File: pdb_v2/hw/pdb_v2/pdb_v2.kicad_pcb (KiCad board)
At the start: 4 copper layers, 92.7 x 64.9 mm, 70 parts, among them J1 XT30-M_Ver, J2 JST-PH_01x02, J3 Conn_01x06_Pin, J5 JST-PH_01x02, J6 Conn_01x03, J7 Conn_01x03, J8 Conn_01x04, Q1 60Vds, SW1 SW_Push, SW2 SW_Push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

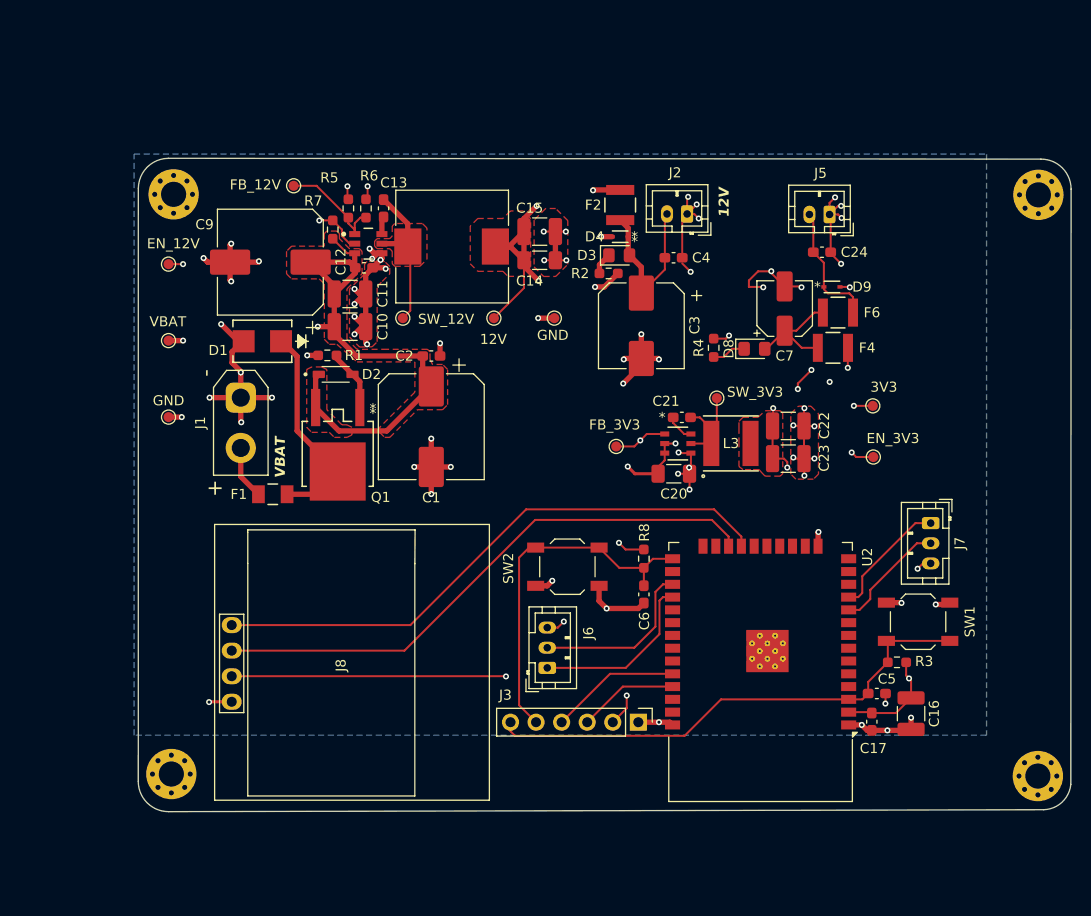
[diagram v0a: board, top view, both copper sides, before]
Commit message: added 2 leds on esp32, moved components
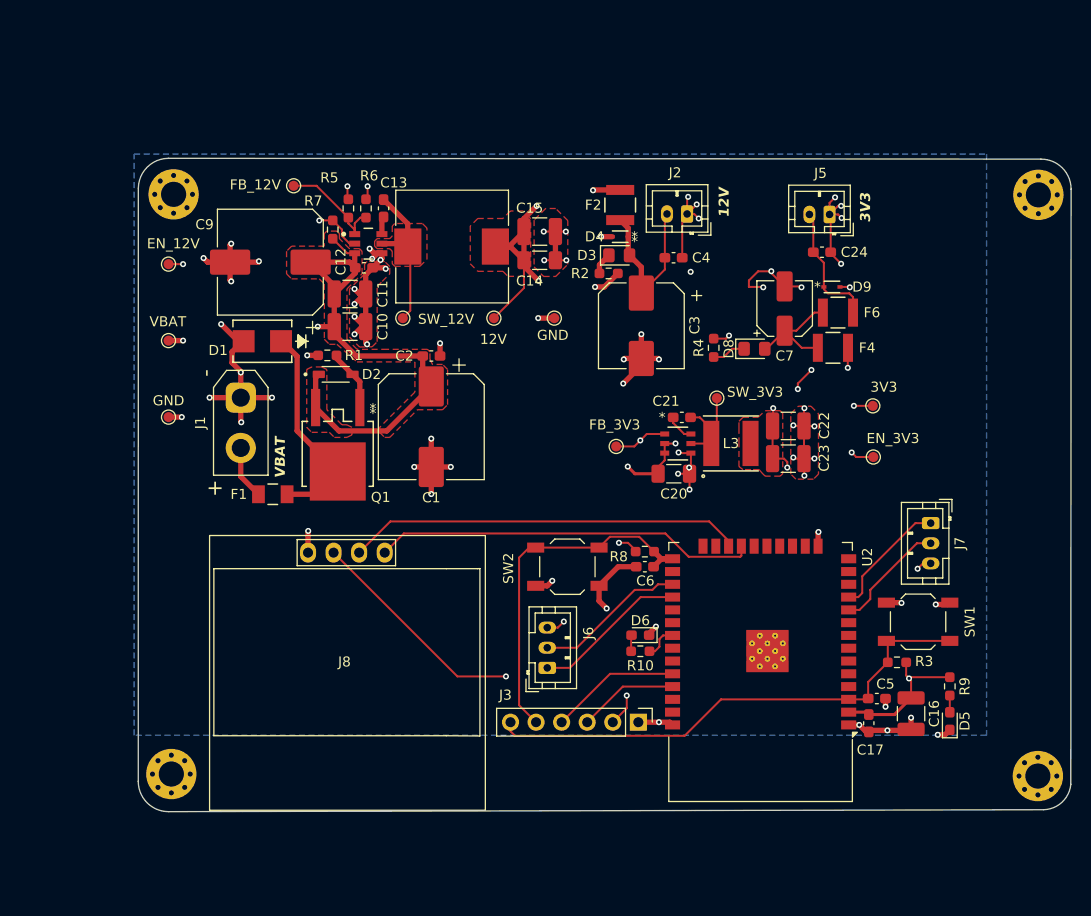
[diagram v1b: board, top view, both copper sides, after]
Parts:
- added D5: LED, LED_SMD:LED_0603_1608Metric_Pad1.05x0.95mm_HandSolder, F.Cu at (92.7, 67.9)
- added D6: LED, LED_SMD:LED_0603_1608Metric_Pad1.05x0.95mm_HandSolder, F.Cu at (61.9, 59.4)
- added R10: 1k, Resistor_SMD:R_0603_1608Metric_Pad0.98x0.95mm_HandSolder, F.Cu at (61.9, 61.0)
- added R9: 1k, Resistor_SMD:R_0603_1608Metric_Pad0.98x0.95mm_HandSolder, F.Cu at (92.7, 64.5)
- moved C6 2.75 mm to (62.4, 52.6), turned to 180 degrees
- moved J8 0.85 mm to (32.5, 61.8), turned to 0 degrees
- moved R8 0.71 mm to (62.4, 51.1), turned to 0 degrees
- moved C5 0.50 mm to (85.4, 65.7)
- moved C17 0.34 mm to (84.6, 68.2)
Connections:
- U2 pad 31: unconnected-(U2-IO19-Pad31) -> Net-(U2-IO19)
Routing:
- net /OLED SDA: track 57.5 -> 38.2 mm
- net /OLED SCL: track 56.4 -> 39.3 mm
- net Net-(U2-IO19): track 0.00 -> 3.39 mm
- net /BMS RX: track 17.1 -> 15.1 mm
- net /BMS TX: track 17.3 -> 15.4 mm
- net GND: track 165.4 -> 167.2 mm, vias 73 -> 75
- net Net-(D5-A): track 0.00 -> 1.66 mm
- net Net-(D6-A): track 0.00 -> 1.62 mm
- net 3V3_BUS: track 158.2 -> 157.1 mm
- net /BOOT: track 35.7 -> 36.3 mm
- net 12V_BUS: track 120.3 -> 119.8 mm, vias 8 -> 7
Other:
- board text added: "3V3"

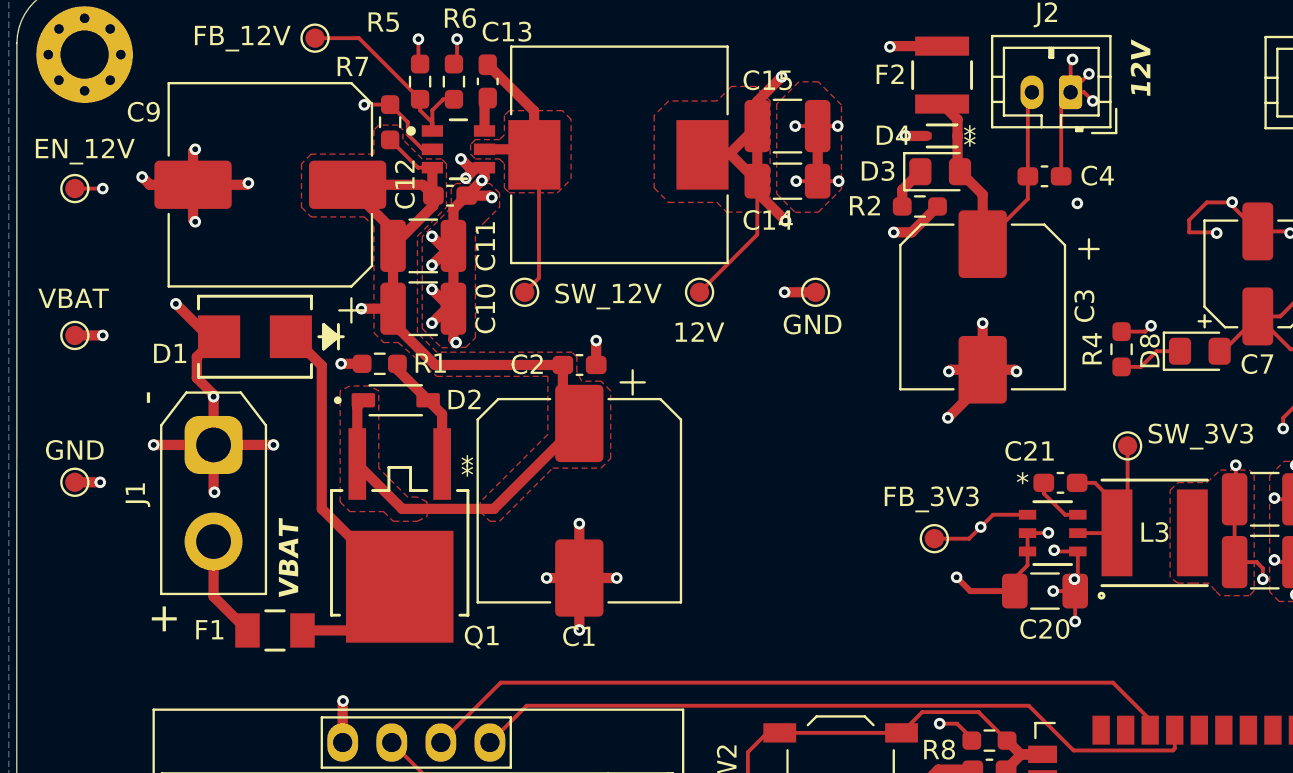
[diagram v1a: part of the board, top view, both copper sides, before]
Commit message: changed J1 footprint
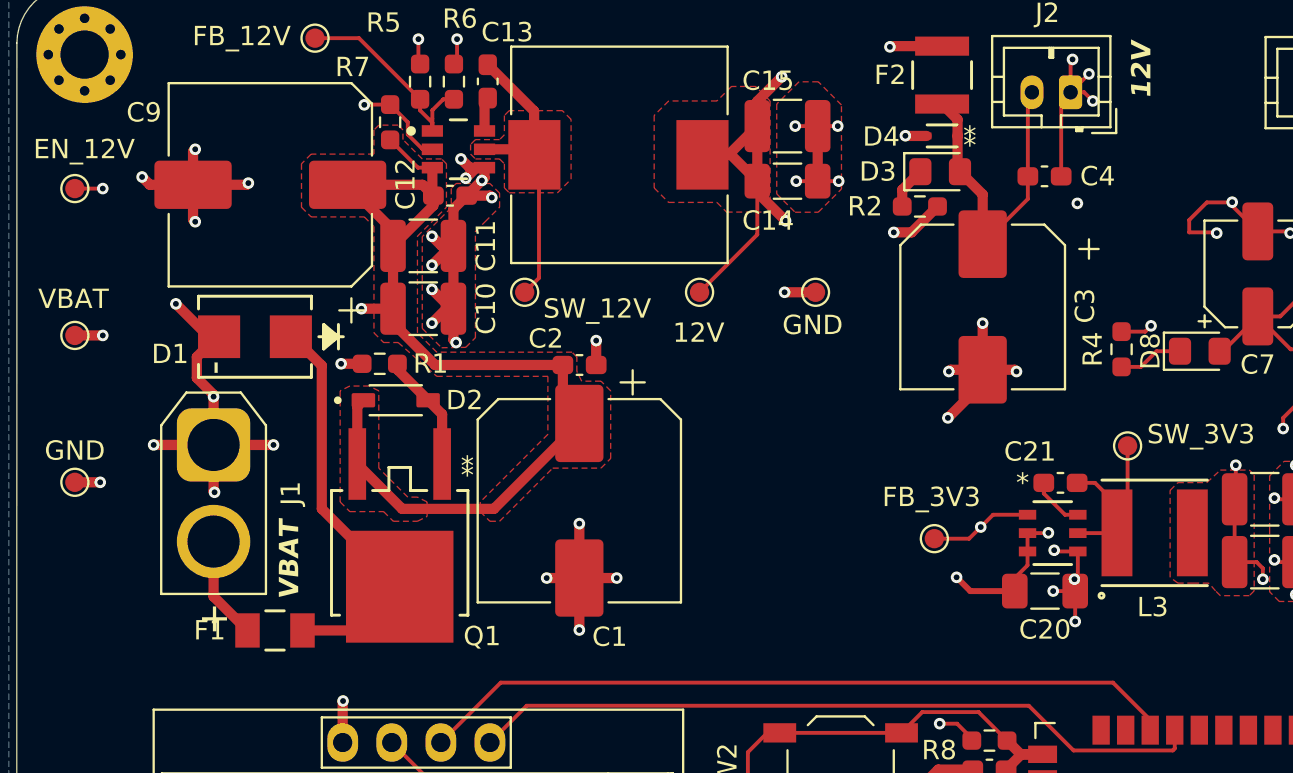
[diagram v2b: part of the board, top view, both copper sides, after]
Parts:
- J1: footprint Connector_AMASS:AMASS_XT30UPB-M_1x02_P5.0mm_Vertical -> Connector_AMASS:AMASS_XT30U-M_1x02_P5.0mm_Vertical
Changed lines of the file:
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@@
 		)
 	)
-	(footprint "Connector_AMASS:AMASS_XT30UPB-M_1x02_P5.0mm_Vertical"
+	(footprint "Connector_AMASS:AMASS_XT30U-M_1x02_P5.0mm_Vertical"
 		(layer "F.Cu")
 		(at 22.2 35.8 -90)
-		(descr "Connector XT30 Vertical PCB Male, https://www.tme.eu/Document/e5863b891432488e7531b3c4468225ac/XT30PB-M.pdf")
+		(descr "Connector XT30 Vertical Cable Male, https://www.tme.eu/Document/7d9d972ae3468777f69ec2ee99897652/XT30U-M.pdf")
 		(tags "RC Connector XT30")
 		(property "Reference" "J1"
-			(at 2.5 4.014998 90)
+			(at 2.5 -4 270)
 			(layer "F.SilkS")
 			(effects
@@
 		)
 		(property "Value" "XT30-M_Ver"
-			(at 2.5 4 90)
+			(at 2.5 4 270)
 			(layer "F.Fab")
 			(effects
@@
 		)
 		(fp_text user "+"
-			(at 9 2.6 90)
+			(at 9 0 270)
 			(layer "F.SilkS")
 			(effects
@@
 		)
 		(fp_text user "-"
-			(at -2.45 3.5 90)
+			(at -4 0 270)
 			(layer "F.SilkS")
 			(effects
@@
 		)
 		(fp_text user "${REFERENCE}"
-			(at 2.5 0 90)
+			(at 2.5 0 270)
 			(layer "F.Fab")
 			(effects
@@
 		(pad "1" thru_hole roundrect
 			(at 0 0 270)
-			(size 3 3)
-			(drill 1.8)
+			(size 3.8 3.8)
+			(drill 2.7)
 			(layers "*.Cu" "*.Mask")
 			(remove_unused_layers no)
-			(roundrect_rratio 0.25)
+			(roundrect_rratio 0.2)
 			(net 2 "GND")
 			(pinfunction "Pin_1")
@@
 		(pad "2" thru_hole circle
 			(at 5 0 270)
-			(size 3 3)
-			(drill 1.8)
+			(size 3.8 3.8)
+			(drill 2.7)
 			(layers "*.Cu" "*.Mask")
 			(remove_unused_layers no)
@@
 		)
 		(embedded_fonts no)
-		(model "C:/Users/Leo/Downloads/Amass_XT30UPB-M.step"
+		(model "${KICAD9_3DMODEL_DIR}/Connector_AMASS.3dshapes/AMASS_XT30U-M_1x02_P5.0mm_Vertical.step"
 			(offset
-				(xyz 2.5 0 0)
+				(xyz 0 0 0)
 			)
 			(scale
@@
 			)
 			(rotate
-				(xyz -0 -0 -0)
+				(xyz 0 0 0)
 			)
 		)
@@
 		(tags "capacitor electrolytic")
 		(property "Reference" "C1"
-			(at 7.05 0 180)
+			(at 7.05 -1.572502 180)
 			(layer "F.SilkS")
 			(effects
@@
 		(tags "capacitor handsolder")
 		(property "Reference" "C2"
-			(at -2.677498 0 0)
+			(at -1.7375 -1.3625 0)
 			(layer "F.SilkS")
 			(effects
@@
 		)
 		(property "Value" "SW_12V"
-			(at 4.3 0.1 0)
+			(at 3.75 0.85 0)
 			(layer "F.SilkS")
 			(effects
@@
 		(tags "ESD5Z12T1G ")
 		(property "Reference" "D4"
-			(at 2.5501 0 0)
+			(at 3.15 -0.0403 0)
 			(unlocked yes)
 			(layer "F.SilkS")
@@
 		(tags "74404052039 ")
 		(property "Reference" "L3"
-			(at 0 0 0)
+			(at -0.1 3.85 0)
 			(unlocked yes)
 			(layer "F.SilkS")

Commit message: final changes for pcb
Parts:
- H1, H2, H3, H4: footprint MountingHole:MountingHole_2.5mm_Pad_Via -> MountingHole:MountingHole_2.5mm_Pad
- moved H2 66.3 mm to (95.1, 81.6)
- moved H4 58.2 mm to (95.1, 15.5)
- moved G*** 16.2 mm to (55.0, 40.5)
- moved H3 8.50 mm to (15.5, 81.7)
- moved C5 6.37 mm to (79.3, 67.5)
- moved C6 6.37 mm to (56.2, 54.4)
- moved D5 6.37 mm to (86.5, 69.7)
- moved J3 6.37 mm to (55.6, 69.8)
- moved J7 6.37 mm to (84.6, 50.0)
- moved R3 6.37 mm to (81.3, 63.9)
- moved R8 6.37 mm to (56.2, 52.9)
- moved R9 6.37 mm to (86.5, 66.2)
- moved SW1 6.37 mm to (83.4, 59.8)
- moved J8 6.37 mm to (26.4, 63.5)
- moved D6 6.37 mm to (55.8, 61.1)
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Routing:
- net 12V_BUS: track 119.8 -> 131.2 mm
- net 3V3_BUS: track 157.1 -> 167.2 mm
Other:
- board size 92.7 x 64.9 mm -> 86.4 x 73.3 mm
- board text added: "Power Distribution Board V2 for F25 Skateboard by Leopoldo Mendoza, Mike Yao, Arnav Shah"
- board text removed: "Power Distribution Board v1 for F25 Skateboard by Leopoldo Mendoza"

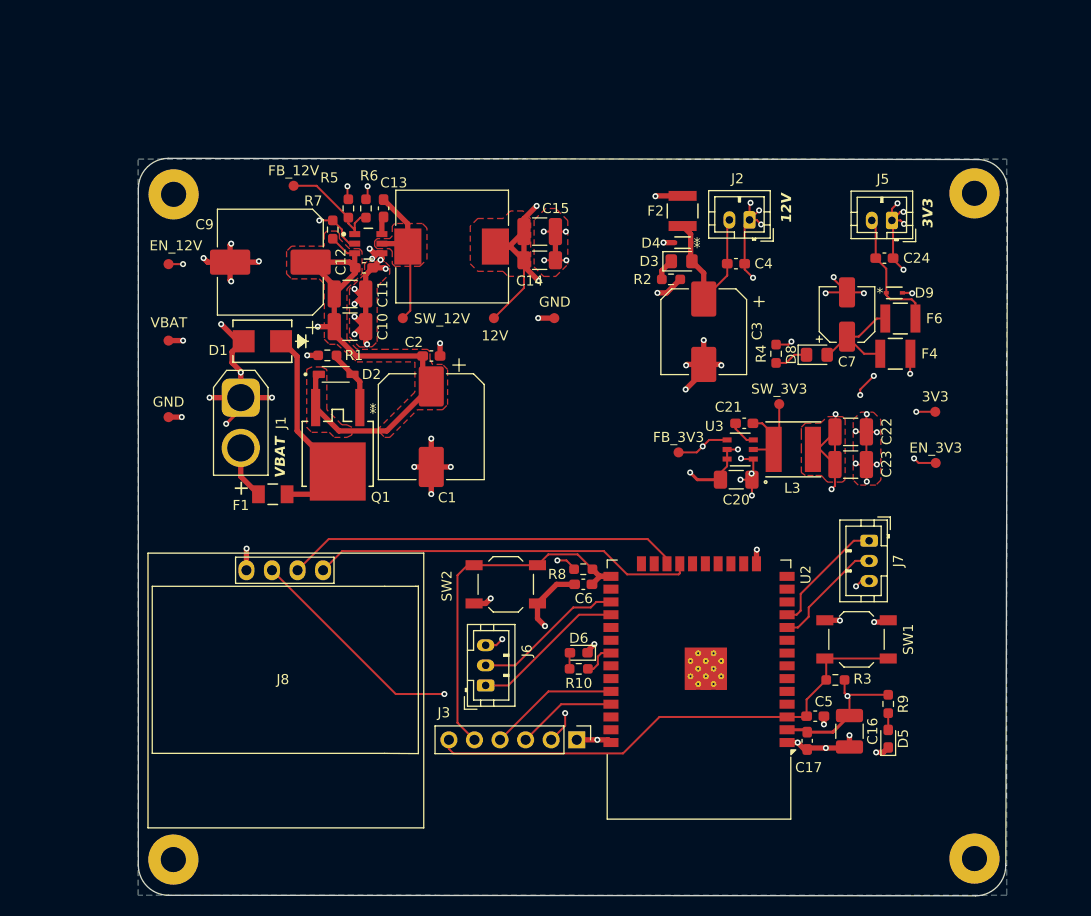
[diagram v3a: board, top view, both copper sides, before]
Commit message: added silkscreen
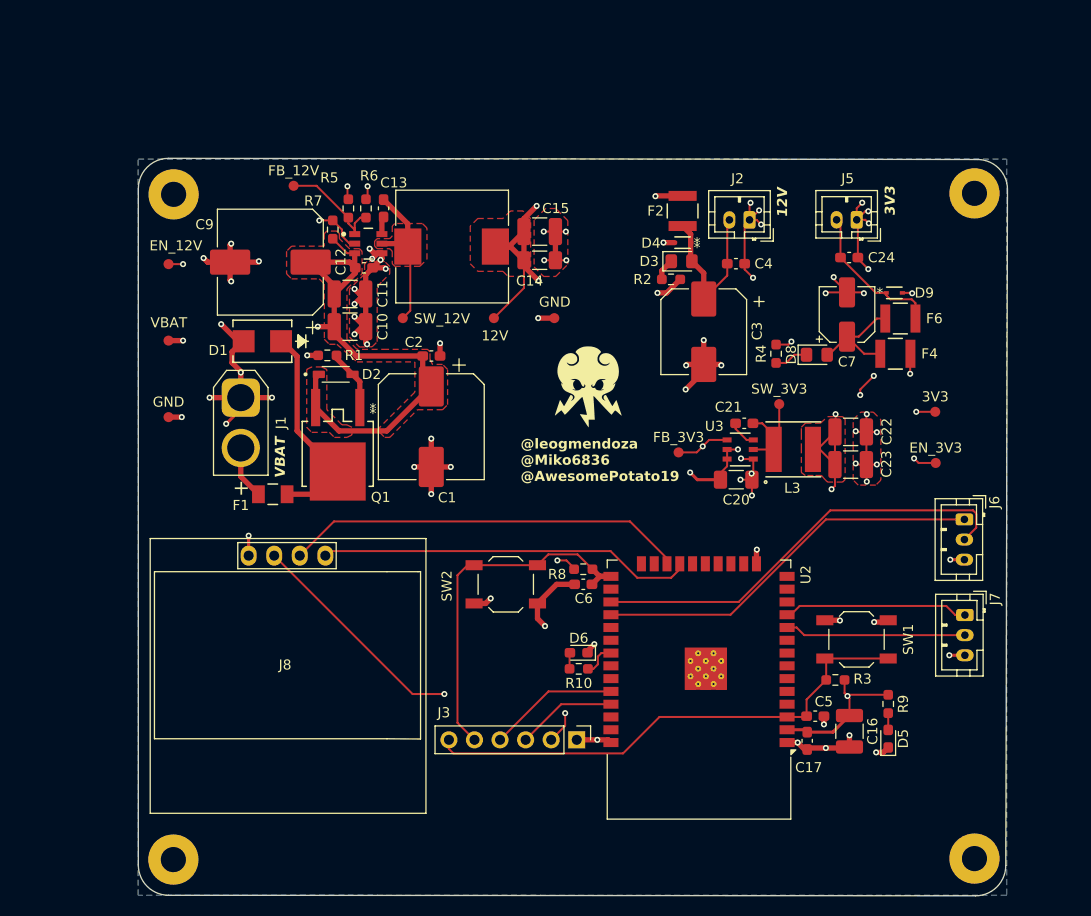
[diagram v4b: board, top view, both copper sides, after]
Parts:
- added G***: LOGO, LOGO, F.Cu at (56.7, 34.7)
- moved J6 50.4 mm to (94.1, 47.9), turned to -90 degrees
- moved J7 12.0 mm to (94.2, 57.4)
- moved C24 3.50 mm to (82.7, 21.9)
- moved J5 3.50 mm to (83.4, 18.1)
- moved G*** 2.00 mm to (55.0, 38.5)
- moved J8 1.47 mm to (26.6, 62.1)
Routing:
- net /BMS RX: track 15.1 -> 43.3 mm
- net /BMS TX: track 15.4 -> 39.0 mm
- net /VESC RX: track 11.4 -> 18.0 mm
- net /VESC TX: track 12.2 -> 18.4 mm
- net Net-(J5-Pin_2): track 12.8 -> 14.9 mm
- net /OLED SDA: track 38.2 -> 37.4 mm
- net GND: track 167.2 -> 166.6 mm
- net /OLED SCL: track 39.3 -> 40.0 mm
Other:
- board text added: "@leogmendoza @Miko6836 @AwesomePotato19"

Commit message: changed silkscreen on back of board
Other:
- board text added: "Power Distribution + Telemetry Board v2 for F25 Skateboard by Leopoldo Mendoza, Mike Yao, Arnav Shah"
- board text removed: "Power Distribution Board V2 for F25 Skateboard by Leopoldo Mendoza, Mike Yao, Arnav Shah"

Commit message: Layout Update
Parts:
- moved J3 38.6 mm to (19.0, 57.4), turned to 0 degrees
- moved C20 8.76 mm to (80.2, 43.8)
- moved C21 8.76 mm to (81.0, 38.2)
- moved C22 8.76 mm to (91.6, 39.1)
- moved C23 8.76 mm to (91.6, 42.3)
- moved C7 8.76 mm to (91.2, 27.4)
- moved D3 8.76 mm to (74.8, 22.1)
- moved D4 8.76 mm to (74.9, 20.2)
- moved D8 8.76 mm to (88.2, 31.4)
- moved EN_3V3 8.76 mm to (100.0, 42.1)
- moved F2 8.76 mm to (74.9, 17.1)
- moved F4 8.76 mm to (96.0, 31.3)
- moved F6 8.76 mm to (96.5, 27.8)
- moved J2 8.76 mm to (81.5, 18.0)
- moved L3 8.76 mm to (85.9, 40.8)
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- renumbered SW2 to BOOT, SW1 to EN
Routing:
- net /TX: track 9.95 -> 47.5 mm, vias 0 -> 1
- net /RX: track 13.0 -> 45.8 mm
- net /EN: track 51.1 -> 80.1 mm
- net /BOOT: track 36.3 -> 60.7 mm, vias 0 -> 1
- net 12V_BUS: track 131.2 -> 148.3 mm
- net /BMS RX: track 43.3 -> 38.6 mm, vias 0 -> 1
- net /OLED SDA: track 37.4 -> 35.1 mm
- net /OLED SCL: track 40.0 -> 38.3 mm
- net 3V3_BUS: track 167.6 -> 166.2 mm, vias 11 -> 9
- net GND: track 166.6 -> 167.4 mm
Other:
- board size 86.4 x 73.3 mm -> 92.1 x 66.3 mm
- board text added: "BOOT"
- board text added: "EN"
- board text added: "GND"
- board text added: "RX"
- board text added: "TX"
